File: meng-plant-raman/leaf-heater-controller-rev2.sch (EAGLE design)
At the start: 15 parts, among them U1 ARDUINOR3-DIMENSION, U2 OPA2333, X1 SM06B-SRSS-TB, X2 SM06B-SRSS-TB

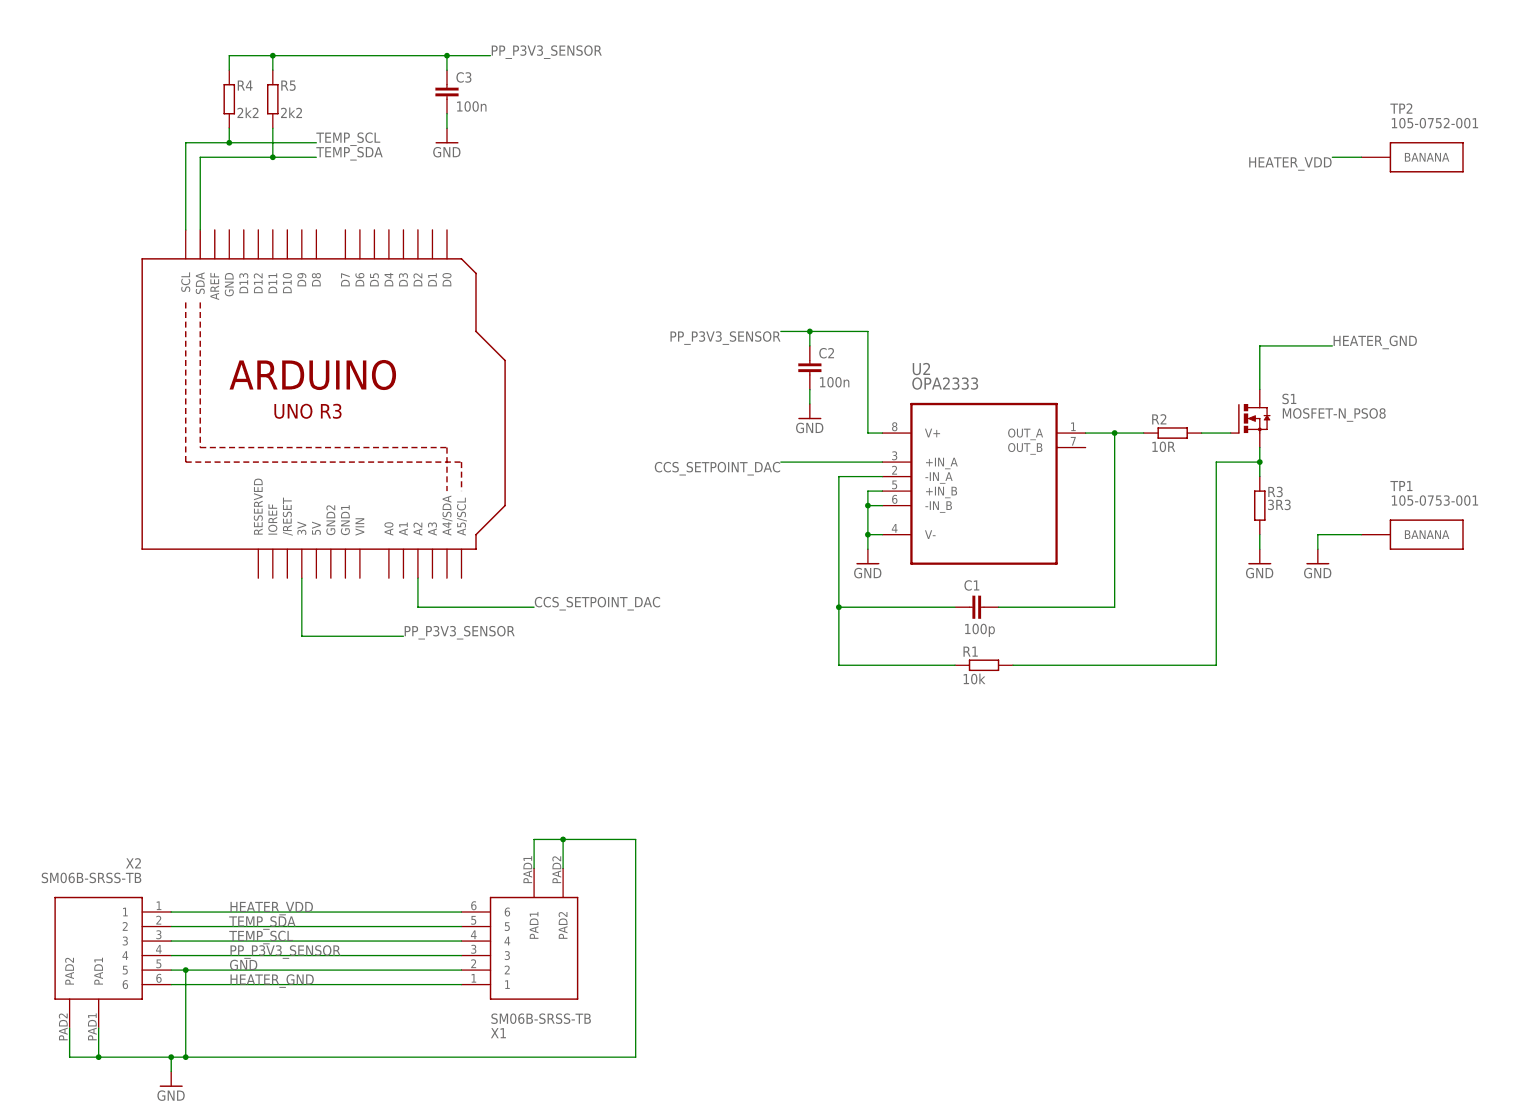
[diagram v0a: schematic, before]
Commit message: Fixed one-shot error, layout done
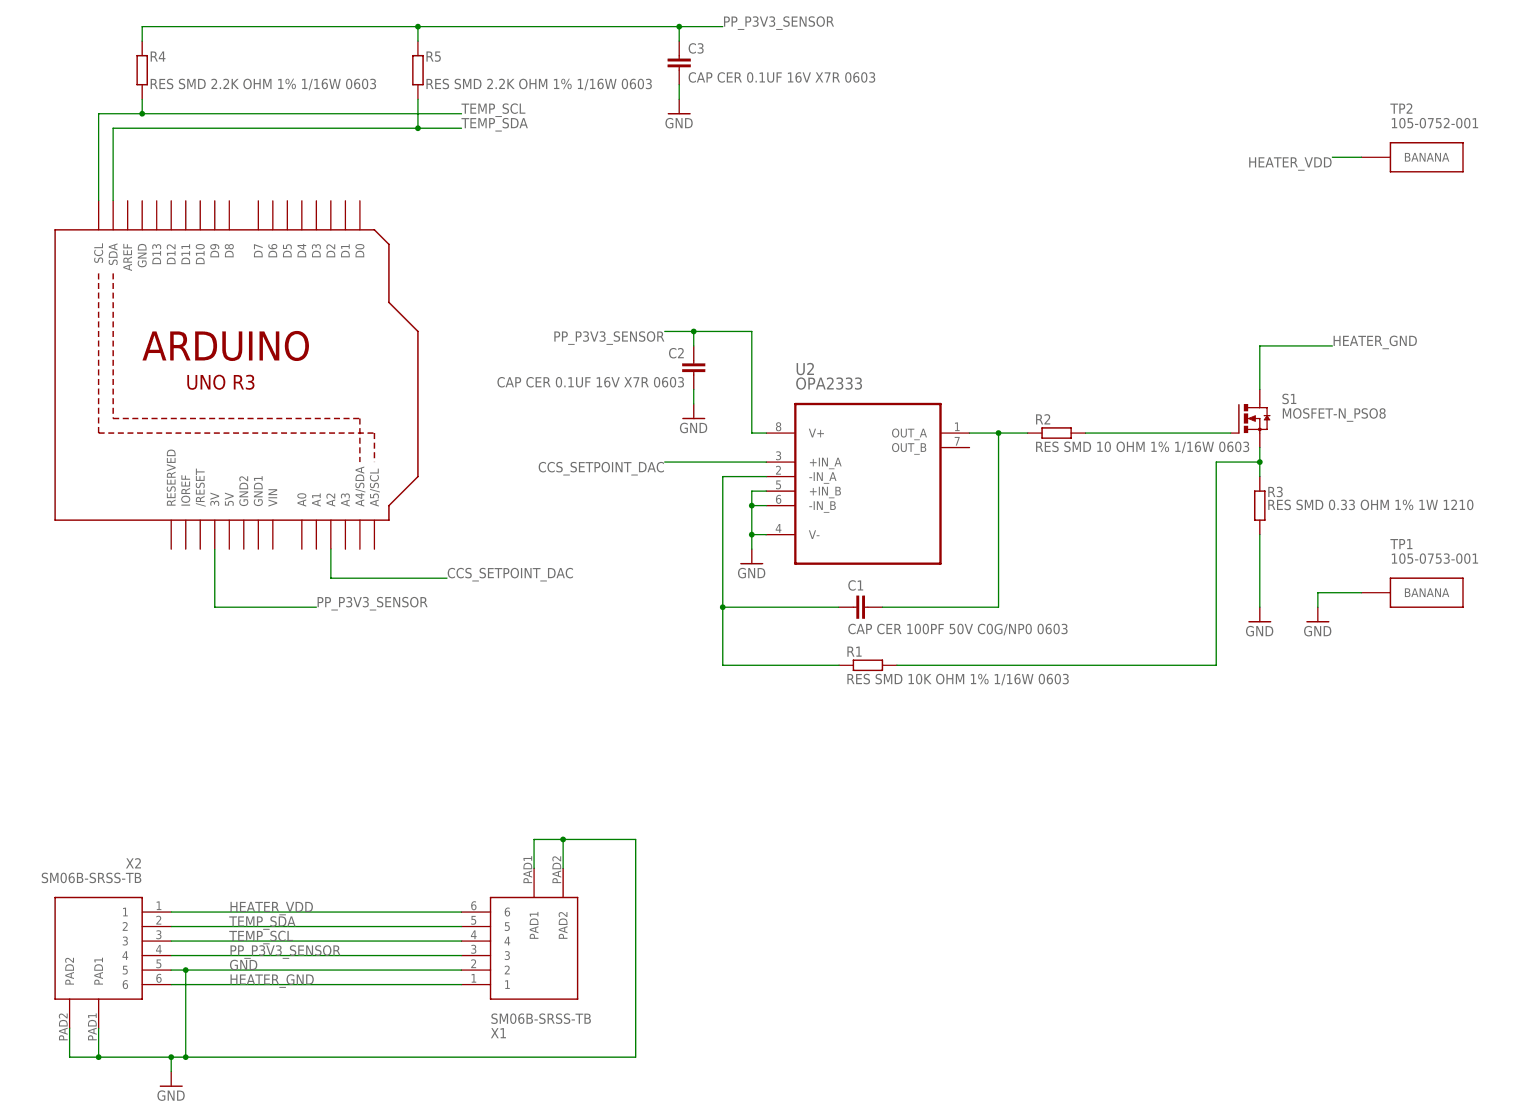
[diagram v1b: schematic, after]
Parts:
- C1: value 100p -> CAP CER 100PF 50V C0G/NP0 0603
- C2, C3: value 100n -> CAP CER 0.1UF 16V X7R 0603
- R1: value 10k -> RES SMD 10K OHM 1% 1/16W 0603
- R2: value 10R -> RES SMD 10 OHM 1% 1/16W 0603
- R3: value 3R3 -> RES SMD 0.33 OHM 1% 1W 1210
- R4, R5: value 2k2 -> RES SMD 2.2K OHM 1% 1/16W 0603
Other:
- moved on the sheet: C1, C2, C3, R1, R2, R4, R5, TP1, U2
